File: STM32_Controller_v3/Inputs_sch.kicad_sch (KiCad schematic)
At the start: 58 parts, among them CN1 WJ15EDGVC-3.5-09P-14-00A, Q1 SMMBT5551LT1G, Q2 SMMBT5551LT1G, Q3 SMMBT5551LT1G, Q4 SMMBT5551LT1G, Q5 SMMBT5551LT1G, Q6 SMMBT5551LT1G, Q7 SMMBT5551LT1G, Q8 SMMBT5551LT1G

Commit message: production version
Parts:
- removed CN1: WJ15EDGVC-3.5-09P-14-00A, Library:PhoenixContact_MCV_1,5_9-G-3.5_1x09_P3.50mm_Vertical, symbol Library:CN_Header_3.5mm_9W_180_300V
- removed CNP1: WJ15EDGK-3.5-09P-14-00A, symbol Library:CN_Plug_3.5mm_9W_180_300V
- added CN1: WJ15EDGVC-3.81-09P-14-00A, Library:PhoenixContact_MCV_1,5_9-G-3.81_1x09_P3.81mm_Vertical, symbol Library:CN_Header_3.81mm_9W_180_300V
- added CNP1: WJ15EDGK-3.81-09P-14-00A, symbol Library:CN_Plug_3.81mm_9W_180_300V
- C1, C2, C3, C4, C5, C6, C7, C8: Assembly (none) -> SMT; Manufacturer (none) -> YAGEO; Part.Number (none) -> CC0805KRX7R9BB104
- LD1, LD2, LD3, LD4, LD5, LD6, LD7, LD8: Assembly (none) -> SMT; Manufacturer (none) -> NATIONSTAR; Part.Number (none) -> NCD0805R1
- Q1, Q2, Q3, Q4, Q5, Q6, Q7, Q8: Assembly (none) -> SMT; Manufacturer (none) -> JSCJ; Part.Number (none) -> MMBT5551
- R1, R10, R11, R12, R17, R19, R21, R23, R25, R26, R27, R28, R3, R5, R7, R9: Assembly (none) -> SMT; Manufacturer (none) -> UNI-ROYAL; Part.Number (none) -> 0805W8F1001T5E
- R13, R14, R15, R16, R18, R2, R20, R22, R24, R29, R30, R31, R32, R4, R6, R8: Assembly (none) -> SMT; Manufacturer (none) -> UNI-ROYAL; Part.Number (none) -> 0805W8F1002T5E
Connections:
- net +V_IN: now also CN1.1 (Pin_1)
- net IN1: now also CN1.2 (Pin_2)
- net IN2: now also CN1.3 (Pin_3)
- net IN3: now also CN1.4 (Pin_4)
- net IN4: now also CN1.5 (Pin_5)
- net IN5: now also CN1.6 (Pin_6)
- net IN6: now also CN1.7 (Pin_7)
- net IN7: now also CN1.8 (Pin_8)
- net IN8: now also CN1.9 (Pin_9)

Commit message: update dimension information
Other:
- note added: "ALTERAR RESISTORES DE BASE PARA 4K7"
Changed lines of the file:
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@@
 		(comment 2 "29/08/2025")
+	)
+	(text "ALTERAR RESISTORES DE BASE PARA 4K7"
+		(exclude_from_sim no)
+		(at 83.566 18.542 0)
+		(effects
+			(font
+				(size 2.54 2.54)
+			)
+		)
 	)
 	(junction

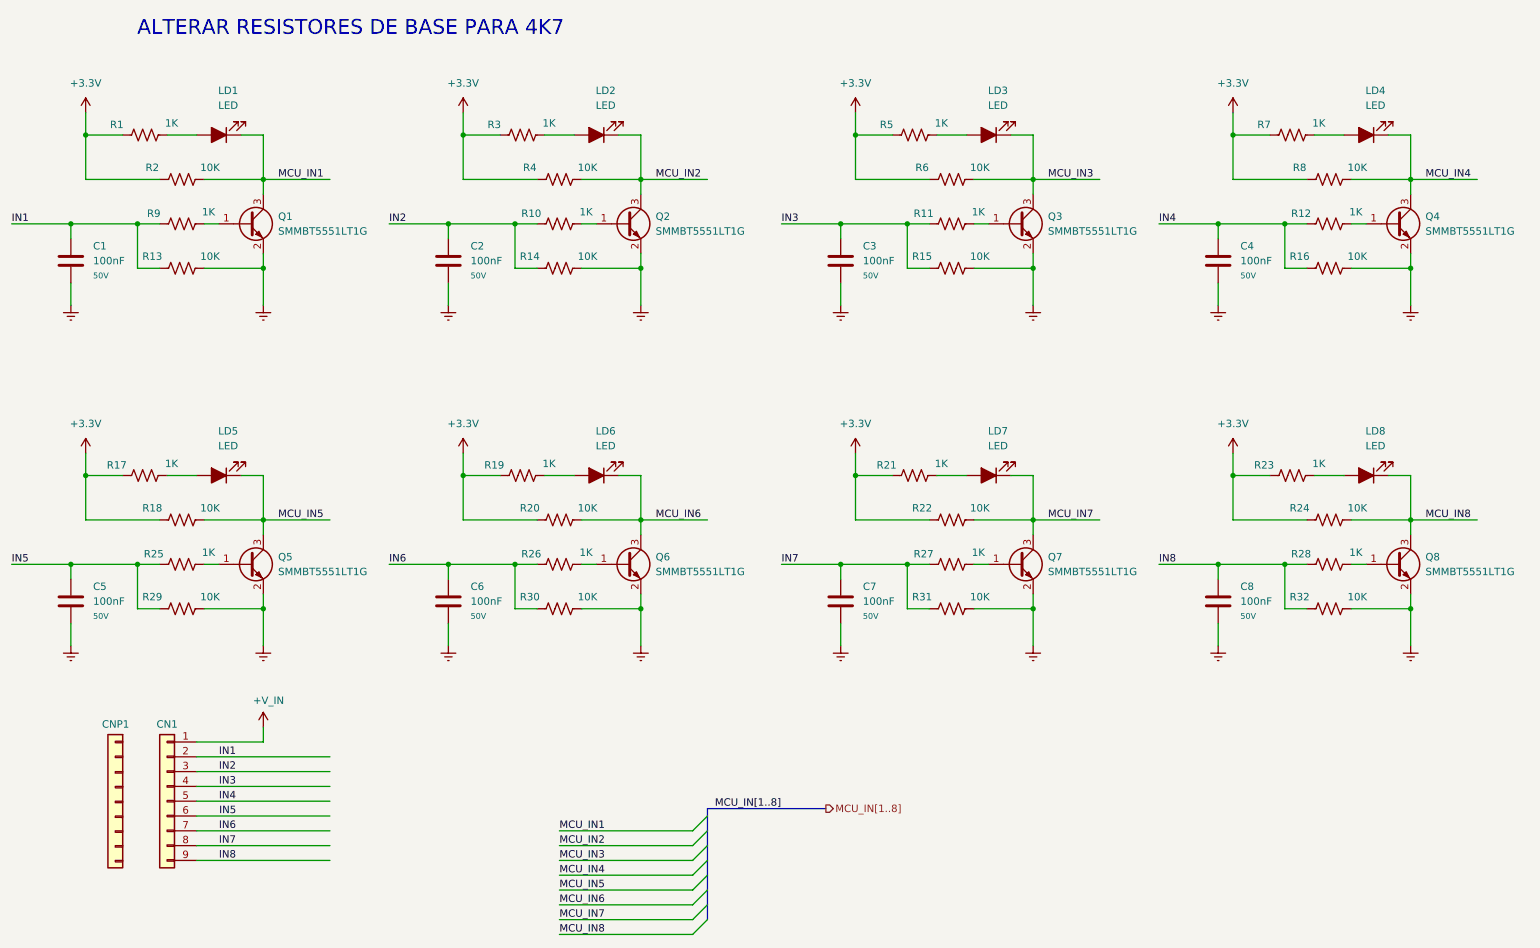
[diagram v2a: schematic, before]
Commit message: res 4k7 in digital inputs and outputs leds
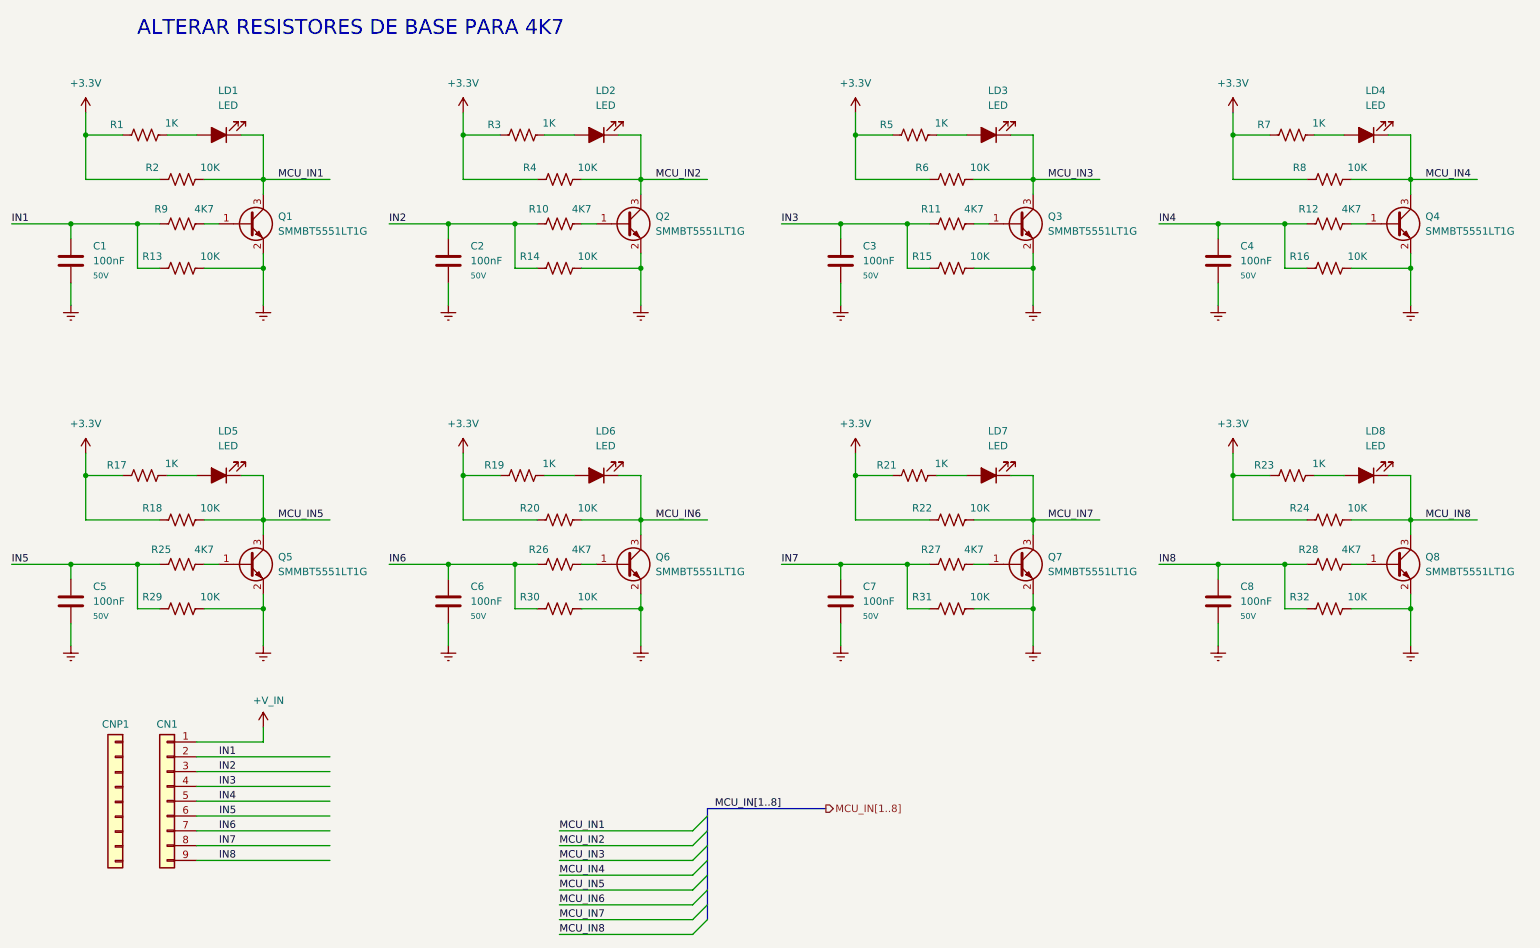
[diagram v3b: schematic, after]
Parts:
- removed R10, R11, R12, R25, R26, R27, R28, R9: 1K, Library:R_0805, symbol Library:R_0805_1K_1P
- added R10, R11, R12, R25, R26, R27, R28, R9: 4K7, db_resistors:R_0805, symbol Library:R_0805_4K7_1P
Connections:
- net IN1: now also R9.1
- net IN2: now also R10.1
- net IN3: now also R11.1
- net IN4: now also R12.1
- net IN5: now also R25.1
- net IN6: now also R26.1
- net IN7: now also R27.1
- net IN8: now also R28.1
- net at Q1.1 (B): now also R9.2
- net at Q5.1 (B): now also R25.2
- net at Q8.1 (B): now also R28.2
- net at Q3.1 (B): now also R11.2
- net at Q7.1 (B): now also R27.2
- net at Q2.1 (B): now also R10.2
- net at Q4.1 (B): now also R12.2
- net at Q6.1 (B): now also R26.2
